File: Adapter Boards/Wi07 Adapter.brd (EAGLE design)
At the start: 24.1 x 24.1 mm, 3 parts, among them U1 WI07-12FULL

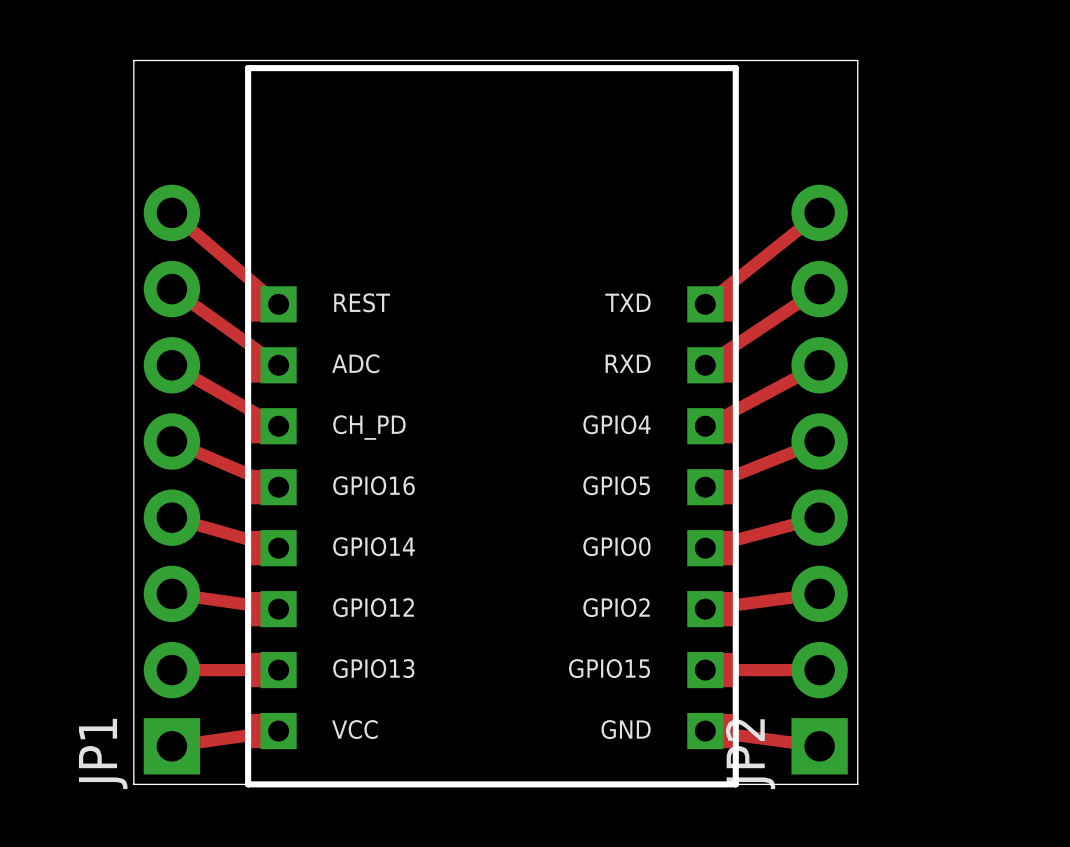
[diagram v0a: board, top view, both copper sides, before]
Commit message: Adding new ESP03 Adapter board; Fix minor errors in library
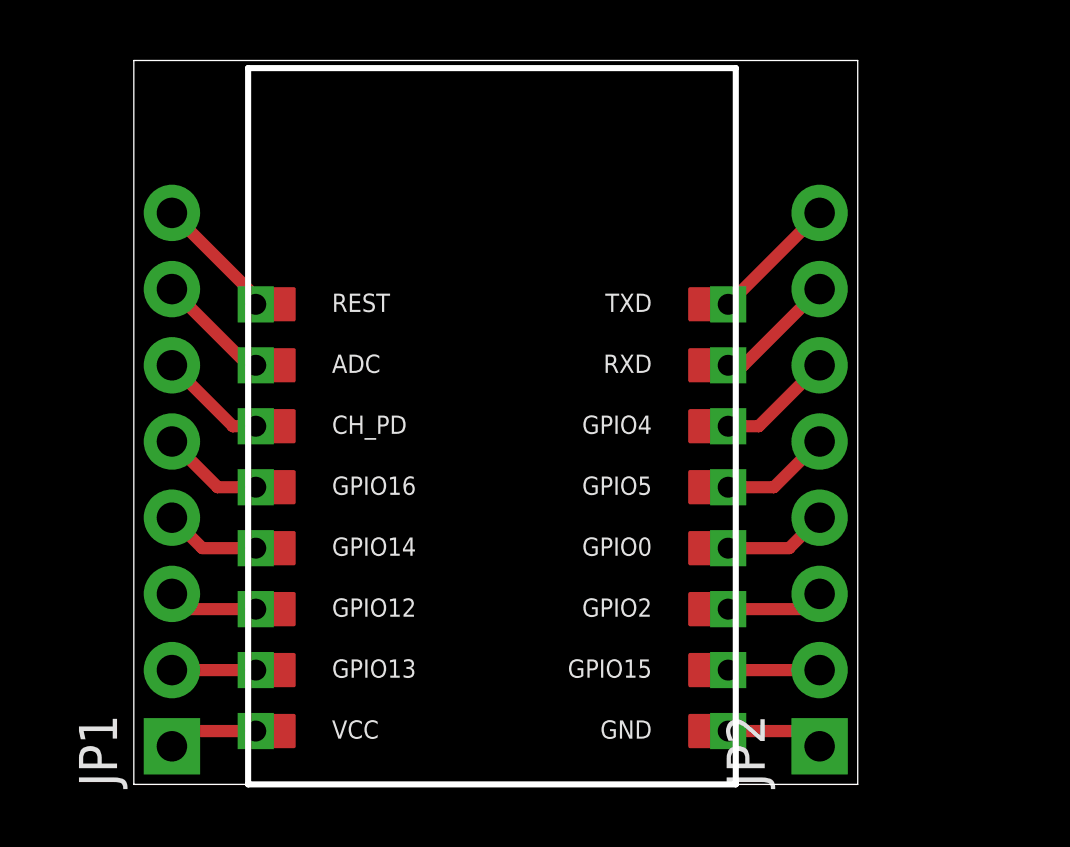
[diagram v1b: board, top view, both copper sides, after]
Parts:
- U1: device Wi07:WI07-12 -> ESP:WI07-12
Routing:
- net N$15: track 3.81 -> 3.05 mm
- net N$2: track 3.56 -> 2.79 mm
- net N$3: track 3.59 -> 3.00 mm
- net N$1: track 3.59 -> 3.00 mm
- net N$16: track 3.84 -> 3.26 mm
- net N$14: track 3.84 -> 3.26 mm
- net N$9: track 4.88 -> 4.31 mm
- net N$7: track 4.37 -> 3.85 mm
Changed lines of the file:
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@@
 <param name="PrefDir.14" value="0"/>
 <param name="PrefDir.15" value="0"/>
-<param name="PrefDir.16" value="a"/>
+<param name="PrefDir.16" value="0"/>
 <param name="cfVia" value="8"/>
 <param name="cfNonPref" value="5"/>
@@
 <element name="JP1" library="SparkFun-Connectors" package="1X08_PIN1_NO_SILK" value="" x="1.27" y="1.27" rot="R90"/>
 <element name="JP2" library="SparkFun-Connectors" package="1X08_PIN1_NO_SILK" value="" x="22.86" y="1.27" rot="R90"/>
-<element name="U1" library="Wi07" package="WI07-12" value="WI07-12FULL" x="3.81" y="0"/>
+<element name="U1" library="ESP" package="WI07-12" value="WI07-12FULL" x="3.81" y="0"/>
 </elements>
 <signals>
@@
 <contactref element="JP1" pad="1"/>
 <contactref element="U1" pad="VCC"/>
-<wire x1="4.826" y1="1.778" x2="1.27" y2="1.27" width="0.4064" layer="1"/>
+<wire x1="4.064" y1="1.778" x2="1.778" y2="1.778" width="0.4064" layer="1"/>
+<wire x1="1.778" y1="1.778" x2="1.27" y2="1.27" width="0.4064" layer="1"/>
 </signal>
 <signal name="N$2">
 <contactref element="JP1" pad="2"/>
 <contactref element="U1" pad="GPIO13"/>
-<wire x1="4.826" y1="3.81" x2="1.27" y2="3.81" width="0.4064" layer="1"/>
+<wire x1="4.064" y1="3.81" x2="1.27" y2="3.81" width="0.4064" layer="1"/>
 </signal>
 <signal name="N$3">
+<contactref element="JP1" pad="3"/>
 <contactref element="U1" pad="GPIO12"/>
-<contactref element="JP1" pad="3"/>
-<wire x1="4.826" y1="5.842" x2="1.27" y2="6.35" width="0.4064" layer="1"/>
+<wire x1="4.064" y1="5.842" x2="1.778" y2="5.842" width="0.4064" layer="1"/>
+<wire x1="1.778" y1="5.842" x2="1.27" y2="6.35" width="0.4064" layer="1"/>
 </signal>
 <signal name="N$4">
 <contactref element="JP1" pad="4"/>
 <contactref element="U1" pad="GPIO14"/>
-<wire x1="4.826" y1="7.874" x2="1.27" y2="8.89" width="0.4064" layer="1"/>
+<wire x1="4.064" y1="7.874" x2="2.286" y2="7.874" width="0.4064" layer="1"/>
+<wire x1="2.286" y1="7.874" x2="1.27" y2="8.89" width="0.4064" layer="1"/>
 </signal>
 <signal name="N$5">
+<contactref element="JP1" pad="5"/>
 <contactref element="U1" pad="GPIO16"/>
-<contactref element="JP1" pad="5"/>
-<wire x1="4.826" y1="9.906" x2="1.27" y2="11.43" width="0.4064" layer="1"/>
+<wire x1="4.064" y1="9.906" x2="2.794" y2="9.906" width="0.4064" layer="1"/>
+<wire x1="2.794" y1="9.906" x2="1.27" y2="11.43" width="0.4064" layer="1"/>
 </signal>
 <signal name="N$6">
 <contactref element="JP1" pad="6"/>
 <contactref element="U1" pad="CH_PD"/>
-<wire x1="4.826" y1="11.938" x2="1.27" y2="13.97" width="0.4064" layer="1"/>
+<wire x1="4.064" y1="11.938" x2="3.302" y2="11.938" width="0.4064" layer="1"/>
+<wire x1="3.302" y1="11.938" x2="1.27" y2="13.97" width="0.4064" layer="1"/>
 </signal>
 <signal name="N$7">
+<contactref element="JP1" pad="7"/>
 <contactref element="U1" pad="ADC"/>
-<contactref element="JP1" pad="7"/>
-<wire x1="4.826" y1="13.97" x2="1.27" y2="16.51" width="0.4064" layer="1"/>
+<wire x1="4.064" y1="13.97" x2="3.81" y2="13.97" width="0.4064" layer="1"/>
+<wire x1="3.81" y1="13.97" x2="1.27" y2="16.51" width="0.4064" layer="1"/>
 </signal>
 <signal name="N$8">
 <contactref element="JP1" pad="8"/>
 <contactref element="U1" pad="REST"/>
-<wire x1="4.826" y1="16.002" x2="1.27" y2="19.05" width="0.4064" layer="1"/>
+<wire x1="4.064" y1="16.002" x2="4.064" y2="16.256" width="0.4064" layer="1"/>
+<wire x1="4.064" y1="16.256" x2="1.27" y2="19.05" width="0.4064" layer="1"/>
 </signal>
 <signal name="N$9">
+<contactref element="JP2" pad="8"/>
 <contactref element="U1" pad="TXD"/>
-<contactref element="JP2" pad="8"/>
-<wire x1="19.05" y1="16.002" x2="22.86" y2="19.05" width="0.4064" layer="1"/>
+<wire x1="19.812" y1="16.002" x2="22.86" y2="19.05" width="0.4064" layer="1"/>
 </signal>
 <signal name="N$10">
 <contactref element="JP2" pad="7"/>
 <contactref element="U1" pad="RXD"/>
-<wire x1="19.05" y1="13.97" x2="22.86" y2="16.51" width="0.4064" layer="1"/>
+<wire x1="19.812" y1="13.97" x2="20.32" y2="13.97" width="0.4064" layer="1"/>
+<wire x1="20.32" y1="13.97" x2="22.86" y2="16.51" width="0.4064" layer="1"/>
 </signal>
 <signal name="N$11">
+<contactref element="JP2" pad="6"/>
 <contactref element="U1" pad="GPIO4"/>
-<contactref element="JP2" pad="6"/>
-<wire x1="19.05" y1="11.938" x2="22.86" y2="13.97" width="0.4064" layer="1"/>
+<wire x1="19.812" y1="11.938" x2="20.828" y2="11.938" width="0.4064" layer="1"/>
+<wire x1="20.828" y1="11.938" x2="22.86" y2="13.97" width="0.4064" layer="1"/>
 </signal>
 <signal name="N$12">
 <contactref element="JP2" pad="5"/>
 <contactref element="U1" pad="GPIO5"/>
-<wire x1="19.05" y1="9.906" x2="22.86" y2="11.43" width="0.4064" layer="1"/>
+<wire x1="19.812" y1="9.906" x2="21.336" y2="9.906" width="0.4064" layer="1"/>
+<wire x1="21.336" y1="9.906" x2="22.86" y2="11.43" width="0.4064" layer="1"/>
 </signal>
 <signal name="N$13">
+<contactref element="JP2" pad="4"/>
 <contactref element="U1" pad="GPIO0"/>
-<contactref element="JP2" pad="4"/>
-<wire x1="19.05" y1="7.874" x2="22.86" y2="8.89" width="0.4064" layer="1"/>
+<wire x1="19.812" y1="7.874" x2="21.844" y2="7.874" width="0.4064" layer="1"/>
+<wire x1="21.844" y1="7.874" x2="22.86" y2="8.89" width="0.4064" layer="1"/>
 </signal>
 <signal name="N$14">
 <contactref element="JP2" pad="3"/>
 <contactref element="U1" pad="GPIO2"/>
-<wire x1="19.05" y1="5.842" x2="22.86" y2="6.35" width="0.4064" layer="1"/>
+<wire x1="19.812" y1="5.842" x2="22.352" y2="5.842" width="0.4064" layer="1"/>
+<wire x1="22.352" y1="5.842" x2="22.86" y2="6.35" width="0.4064" layer="1"/>
 </signal>
 <signal name="N$15">
+<contactref element="JP2" pad="2"/>
 <contactref element="U1" pad="GPIO15"/>
-<contactref element="JP2" pad="2"/>
-<wire x1="19.05" y1="3.81" x2="22.86" y2="3.81" width="0.4064" layer="1"/>
+<wire x1="19.812" y1="3.81" x2="22.86" y2="3.81" width="0.4064" layer="1"/>
 </signal>
 <signal name="N$16">
 <contactref element="JP2" pad="1"/>
 <contactref element="U1" pad="GND"/>
-<wire x1="19.05" y1="1.778" x2="22.86" y2="1.27" width="0.4064" layer="1"/>
+<wire x1="19.812" y1="1.778" x2="22.352" y2="1.778" width="0.4064" layer="1"/>
+<wire x1="22.352" y1="1.778" x2="22.86" y2="1.27" width="0.4064" layer="1"/>
 </signal>
 </signals>

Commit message: Added OSHW logos
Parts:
- added U$1: (no value), SparkFun-Aesthetics:OSHW-LOGO-M
- moved JP2 1.27 mm to (24.1, 1.27)
- moved U1 0.64 mm to (4.45, 0.00)
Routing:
- net N$15: track 3.05 -> 3.68 mm
- net N$5: track 3.43 -> 4.06 mm
- net N$7: track 3.85 -> 4.48 mm
- net N$6: track 3.64 -> 4.27 mm
- net N$4: track 3.21 -> 3.85 mm
- net N$3: track 3.00 -> 3.64 mm
- net N$2: track 2.79 -> 3.43 mm
- net N$1: track 3.00 -> 3.64 mm
- net N$10: track 4.10 -> 4.71 mm
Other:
- board size 24.1 x 24.1 mm -> 25.4 x 24.1 mm
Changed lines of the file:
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@@
 <layer number="25" name="tNames" color="7" fill="1" visible="yes" active="yes"/>
 <layer number="26" name="bNames" color="7" fill="1" visible="yes" active="yes"/>
-<layer number="27" name="tValues" color="7" fill="1" visible="yes" active="yes"/>
-<layer number="28" name="bValues" color="7" fill="1" visible="yes" active="yes"/>
+<layer number="27" name="tValues" color="7" fill="1" visible="no" active="yes"/>
+<layer number="28" name="bValues" color="7" fill="1" visible="no" active="yes"/>
 <layer number="29" name="tStop" color="7" fill="3" visible="no" active="yes"/>
 <layer number="30" name="bStop" color="7" fill="6" visible="no" active="yes"/>
@@
 <board>
 <plain>
-<wire x1="0" y1="0" x2="24.13" y2="0" width="0" layer="20"/>
-<wire x1="24.13" y1="0" x2="24.13" y2="24.13" width="0" layer="20"/>
-<wire x1="24.13" y1="24.13" x2="0" y2="24.13" width="0" layer="20"/>
+<wire x1="0" y1="0" x2="25.4" y2="0" width="0" layer="20"/>
+<wire x1="25.4" y1="0" x2="25.4" y2="24.13" width="0" layer="20"/>
+<wire x1="25.4" y1="24.13" x2="0" y2="24.13" width="0" layer="20"/>
 <wire x1="0" y1="24.13" x2="0" y2="0" width="0" layer="20"/>
 </plain>
@@
 </autorouter>
 <elements>
-<element name="JP1" library="SparkFun-Connectors" package="1X08_PIN1_NO_SILK" value="" x="1.27" y="1.27" rot="R90"/>
-<element name="JP2" library="SparkFun-Connectors" package="1X08_PIN1_NO_SILK" value="" x="22.86" y="1.27" rot="R90"/>
-<element name="U1" library="ESP" package="WI07-12" value="WI07-12FULL" x="3.81" y="0"/>
+<element name="JP1" library="SparkFun-Connectors" package="1X08_PIN1_NO_SILK" value="" x="1.27" y="1.27" smashed="yes" rot="R90">
+<attribute name="NAME" x="-0.5588" y="-0.0762" size="1.27" layer="27" ratio="10" rot="R90"/>
+<attribute name="VALUE" x="4.445" y="0" size="1.27" layer="27" rot="R90"/>
+</element>
+<element name="JP2" library="SparkFun-Connectors" package="1X08_PIN1_NO_SILK" value="" x="24.13" y="1.27" smashed="yes" rot="R90">
+<attribute name="NAME" x="22.3012" y="-0.0762" size="1.27" layer="27" ratio="10" rot="R90"/>
+<attribute name="VALUE" x="27.305" y="0" size="1.27" layer="27" rot="R90"/>
+</element>
+<element name="U1" library="ESP" package="WI07-12" value="WI07-12FULL" x="4.445" y="0"/>
+<element name="U$1" library="SparkFun-Aesthetics" package="OSHW-LOGO-M" value="" x="17.78" y="20.32"/>
 </elements>
 <signals>
@@
 <contactref element="JP1" pad="1"/>
 <contactref element="U1" pad="VCC"/>
-<wire x1="4.064" y1="1.778" x2="1.778" y2="1.778" width="0.4064" layer="1"/>
+<wire x1="4.699" y1="1.778" x2="1.778" y2="1.778" width="0.4064" layer="1"/>
 <wire x1="1.778" y1="1.778" x2="1.27" y2="1.27" width="0.4064" layer="1"/>
 </signal>
@@
 <contactref element="JP1" pad="2"/>
 <contactref element="U1" pad="GPIO13"/>
-<wire x1="4.064" y1="3.81" x2="1.27" y2="3.81" width="0.4064" layer="1"/>
+<wire x1="4.699" y1="3.81" x2="1.27" y2="3.81" width="0.4064" layer="1"/>
 </signal>
 <signal name="N$3">
 <contactref element="JP1" pad="3"/>
 <contactref element="U1" pad="GPIO12"/>
-<wire x1="4.064" y1="5.842" x2="1.778" y2="5.842" width="0.4064" layer="1"/>
+<wire x1="4.699" y1="5.842" x2="1.778" y2="5.842" width="0.4064" layer="1"/>
 <wire x1="1.778" y1="5.842" x2="1.27" y2="6.35" width="0.4064" layer="1"/>
 </signal>
@@
 <contactref element="JP1" pad="4"/>
 <contactref element="U1" pad="GPIO14"/>
-<wire x1="4.064" y1="7.874" x2="2.286" y2="7.874" width="0.4064" layer="1"/>
+<wire x1="4.699" y1="7.874" x2="2.286" y2="7.874" width="0.4064" layer="1"/>
 <wire x1="2.286" y1="7.874" x2="1.27" y2="8.89" width="0.4064" layer="1"/>
 </signal>
@@
 <contactref element="JP1" pad="5"/>
 <contactref element="U1" pad="GPIO16"/>
-<wire x1="4.064" y1="9.906" x2="2.794" y2="9.906" width="0.4064" layer="1"/>
+<wire x1="4.699" y1="9.906" x2="2.794" y2="9.906" width="0.4064" layer="1"/>
 <wire x1="2.794" y1="9.906" x2="1.27" y2="11.43" width="0.4064" layer="1"/>
 </signal>
@@
 <contactref element="JP1" pad="6"/>
 <contactref element="U1" pad="CH_PD"/>
-<wire x1="4.064" y1="11.938" x2="3.302" y2="11.938" width="0.4064" layer="1"/>
+<wire x1="4.699" y1="11.938" x2="3.302" y2="11.938" width="0.4064" layer="1"/>
 <wire x1="3.302" y1="11.938" x2="1.27" y2="13.97" width="0.4064" layer="1"/>
 </signal>
@@
 <contactref element="JP1" pad="7"/>
 <contactref element="U1" pad="ADC"/>
-<wire x1="4.064" y1="13.97" x2="3.81" y2="13.97" width="0.4064" layer="1"/>
+<wire x1="4.699" y1="13.97" x2="3.81" y2="13.97" width="0.4064" layer="1"/>
 <wire x1="3.81" y1="13.97" x2="1.27" y2="16.51" width="0.4064" layer="1"/>
 </signal>
@@
 <contactref element="JP1" pad="8"/>
 <contactref element="U1" pad="REST"/>
-<wire x1="4.064" y1="16.002" x2="4.064" y2="16.256" width="0.4064" layer="1"/>
+<wire x1="4.699" y1="16.002" x2="4.064" y2="16.256" width="0.4064" layer="1"/>
 <wire x1="4.064" y1="16.256" x2="1.27" y2="19.05" width="0.4064" layer="1"/>
 </signal>
@@
 <contactref element="JP2" pad="8"/>
 <contactref element="U1" pad="TXD"/>
-<wire x1="19.812" y1="16.002" x2="22.86" y2="19.05" width="0.4064" layer="1"/>
+<wire x1="20.447" y1="16.002" x2="24.13" y2="19.05" width="0.4064" layer="1"/>
 </signal>
 <signal name="N$10">
 <contactref element="JP2" pad="7"/>
 <contactref element="U1" pad="RXD"/>
-<wire x1="19.812" y1="13.97" x2="20.32" y2="13.97" width="0.4064" layer="1"/>
-<wire x1="20.32" y1="13.97" x2="22.86" y2="16.51" width="0.4064" layer="1"/>
+<wire x1="20.447" y1="13.97" x2="20.32" y2="13.97" width="0.4064" layer="1"/>
+<wire x1="20.32" y1="13.97" x2="24.13" y2="16.51" width="0.4064" layer="1"/>
 </signal>
 <signal name="N$11">
 <contactref element="JP2" pad="6"/>
 <contactref element="U1" pad="GPIO4"/>
-<wire x1="19.812" y1="11.938" x2="20.828" y2="11.938" width="0.4064" layer="1"/>
-<wire x1="20.828" y1="11.938" x2="22.86" y2="13.97" width="0.4064" layer="1"/>
+<wire x1="20.447" y1="11.938" x2="20.828" y2="11.938" width="0.4064" layer="1"/>
+<wire x1="20.828" y1="11.938" x2="24.13" y2="13.97" width="0.4064" layer="1"/>
 </signal>
 <signal name="N$12">
 <contactref element="JP2" pad="5"/>
 <contactref element="U1" pad="GPIO5"/>
-<wire x1="19.812" y1="9.906" x2="21.336" y2="9.906" width="0.4064" layer="1"/>
-<wire x1="21.336" y1="9.906" x2="22.86" y2="11.43" width="0.4064" layer="1"/>
+<wire x1="20.447" y1="9.906" x2="21.336" y2="9.906" width="0.4064" layer="1"/>
+<wire x1="21.336" y1="9.906" x2="24.13" y2="11.43" width="0.4064" layer="1"/>
 </signal>
 <signal name="N$13">
 <contactref element="JP2" pad="4"/>
 <contactref element="U1" pad="GPIO0"/>
-<wire x1="19.812" y1="7.874" x2="21.844" y2="7.874" width="0.4064" layer="1"/>
-<wire x1="21.844" y1="7.874" x2="22.86" y2="8.89" width="0.4064" layer="1"/>
+<wire x1="20.447" y1="7.874" x2="21.844" y2="7.874" width="0.4064" layer="1"/>
+<wire x1="21.844" y1="7.874" x2="24.13" y2="8.89" width="0.4064" layer="1"/>
 </signal>
 <signal name="N$14">
 <contactref element="JP2" pad="3"/>
 <contactref element="U1" pad="GPIO2"/>
-<wire x1="19.812" y1="5.842" x2="22.352" y2="5.842" width="0.4064" layer="1"/>
-<wire x1="22.352" y1="5.842" x2="22.86" y2="6.35" width="0.4064" layer="1"/>
+<wire x1="20.447" y1="5.842" x2="22.352" y2="5.842" width="0.4064" layer="1"/>
+<wire x1="22.352" y1="5.842" x2="24.13" y2="6.35" width="0.4064" layer="1"/>
 </signal>
 <signal name="N$15">
 <contactref element="JP2" pad="2"/>
 <contactref element="U1" pad="GPIO15"/>
-<wire x1="19.812" y1="3.81" x2="22.86" y2="3.81" width="0.4064" layer="1"/>
+<wire x1="20.447" y1="3.81" x2="24.13" y2="3.81" width="0.4064" layer="1"/>
 </signal>
 <signal name="N$16">
 <contactref element="JP2" pad="1"/>
 <contactref element="U1" pad="GND"/>
-<wire x1="19.812" y1="1.778" x2="22.352" y2="1.778" width="0.4064" layer="1"/>
-<wire x1="22.352" y1="1.778" x2="22.86" y2="1.27" width="0.4064" layer="1"/>
+<wire x1="20.447" y1="1.778" x2="22.352" y2="1.778" width="0.4064" layer="1"/>
+<wire x1="22.352" y1="1.778" x2="24.13" y2="1.27" width="0.4064" layer="1"/>
 </signal>
 </signals>

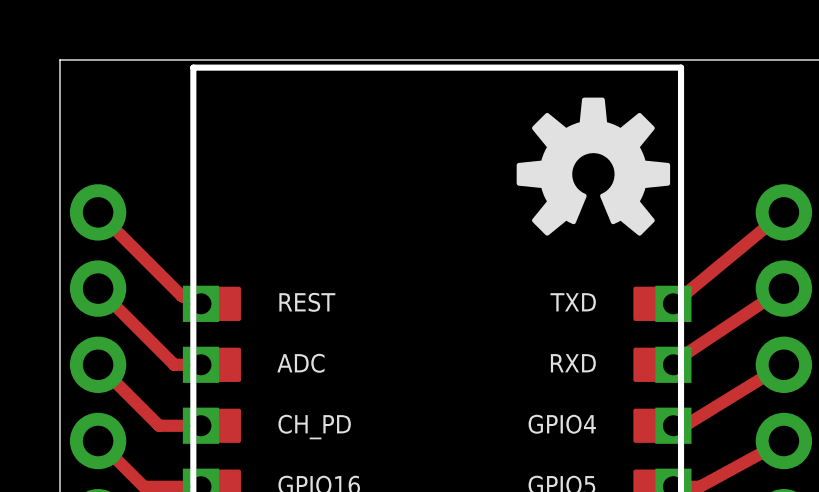
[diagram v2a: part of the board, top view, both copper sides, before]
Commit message: Added hark logo
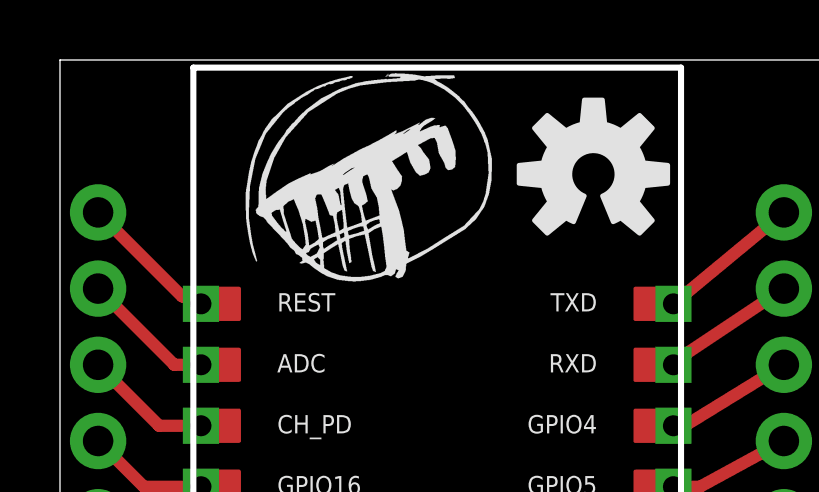
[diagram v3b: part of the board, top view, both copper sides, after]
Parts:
- added E$1: (no value), ESP:HARK
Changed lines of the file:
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@@
 <element name="U1" library="ESP" package="WI07-12" value="WI07-12FULL" x="4.445" y="0"/>
 <element name="U$1" library="SparkFun-Aesthetics" package="OSHW-LOGO-M" value="" x="17.78" y="20.32"/>
+<element name="E$1" library="ESP" package="HARK" value="" x="5.715" y="16.51"/>
 </elements>
 <signals>
